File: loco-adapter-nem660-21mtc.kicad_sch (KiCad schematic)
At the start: 1 part, among them J401 Conn_02x11_Odd_Even

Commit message: Fix - ERC updates
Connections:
- no-connect marks 1 -> 11
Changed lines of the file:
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@@
+	)
+	(no_connect
+		(at 77.47 91.44)
+	)
+	(no_connect
+		(at 40.64 101.6)
+	)
+	(no_connect
+		(at 40.64 86.36)
+	)
+	(no_connect
+		(at 82.55 99.06)
+	)
+	(no_connect
+		(at 40.64 99.06)
+	)
+	(no_connect
+		(at 40.64 78.74)
 	)
 	(no_connect
 		(at 53.34 104.14)
 	)
+	(no_connect
+		(at 40.64 81.28)
+	)
+	(no_connect
+		(at 82.55 101.6)
+	)
+	(no_connect
+		(at 82.55 96.52)
+	)
+	(no_connect
+		(at 40.64 83.82)
+	)
 	(wire

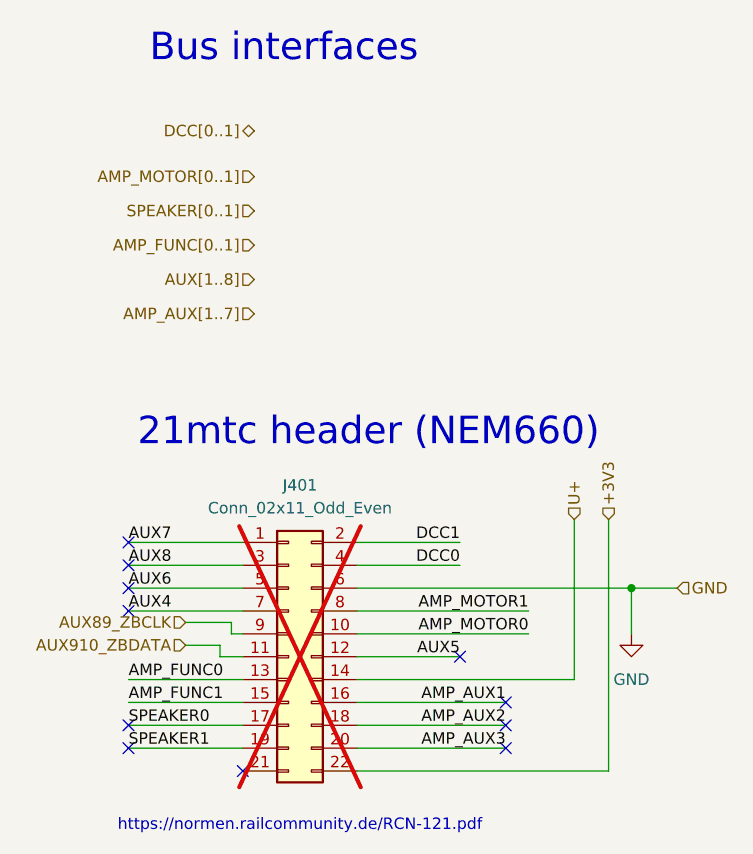
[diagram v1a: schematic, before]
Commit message: Fix - Ignore double power flags
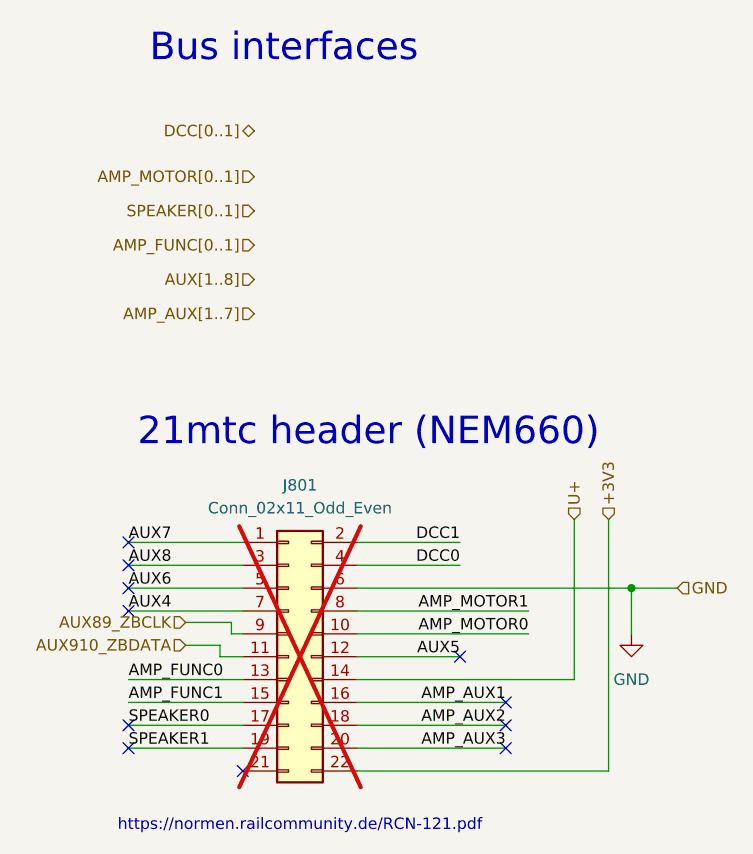
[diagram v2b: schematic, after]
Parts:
- renumbered J401 to J801
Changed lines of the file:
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@@
 		(dnp yes)
 		(fields_autoplaced yes)
-		(property "Reference" "J401"
+		(property "Reference" "J801"
 			(at 59.69 72.39 0)
 			(effects
@@
 			(project ""
 				(path "/fb33ec4e-6596-45d2-a121-8d3475acd69a/3c699e35-5808-46af-b922-4c3eb1f6da5c"
-					(reference "J401")
+					(reference "J801")
 					(unit 1)
 				)
@@
 			(project "loco-adapter-nem660-21mtc"
 				(path "/fb33ec4e-6596-45d2-a121-8d3475acd69a/3c699e35-5808-46af-b922-4c3eb1f6da5c"
-					(reference "#PWR401")
+					(reference "#PWR801")
 					(unit 1)
 				)
